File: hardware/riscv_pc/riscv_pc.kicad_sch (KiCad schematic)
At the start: 14 parts, among them J1 te_m.2_b, J2 te_m.2_b, J3 Conn_01x06, J4 HDMI_A, J5 AudioJack3, SW1 TS-1187A-C-D-B

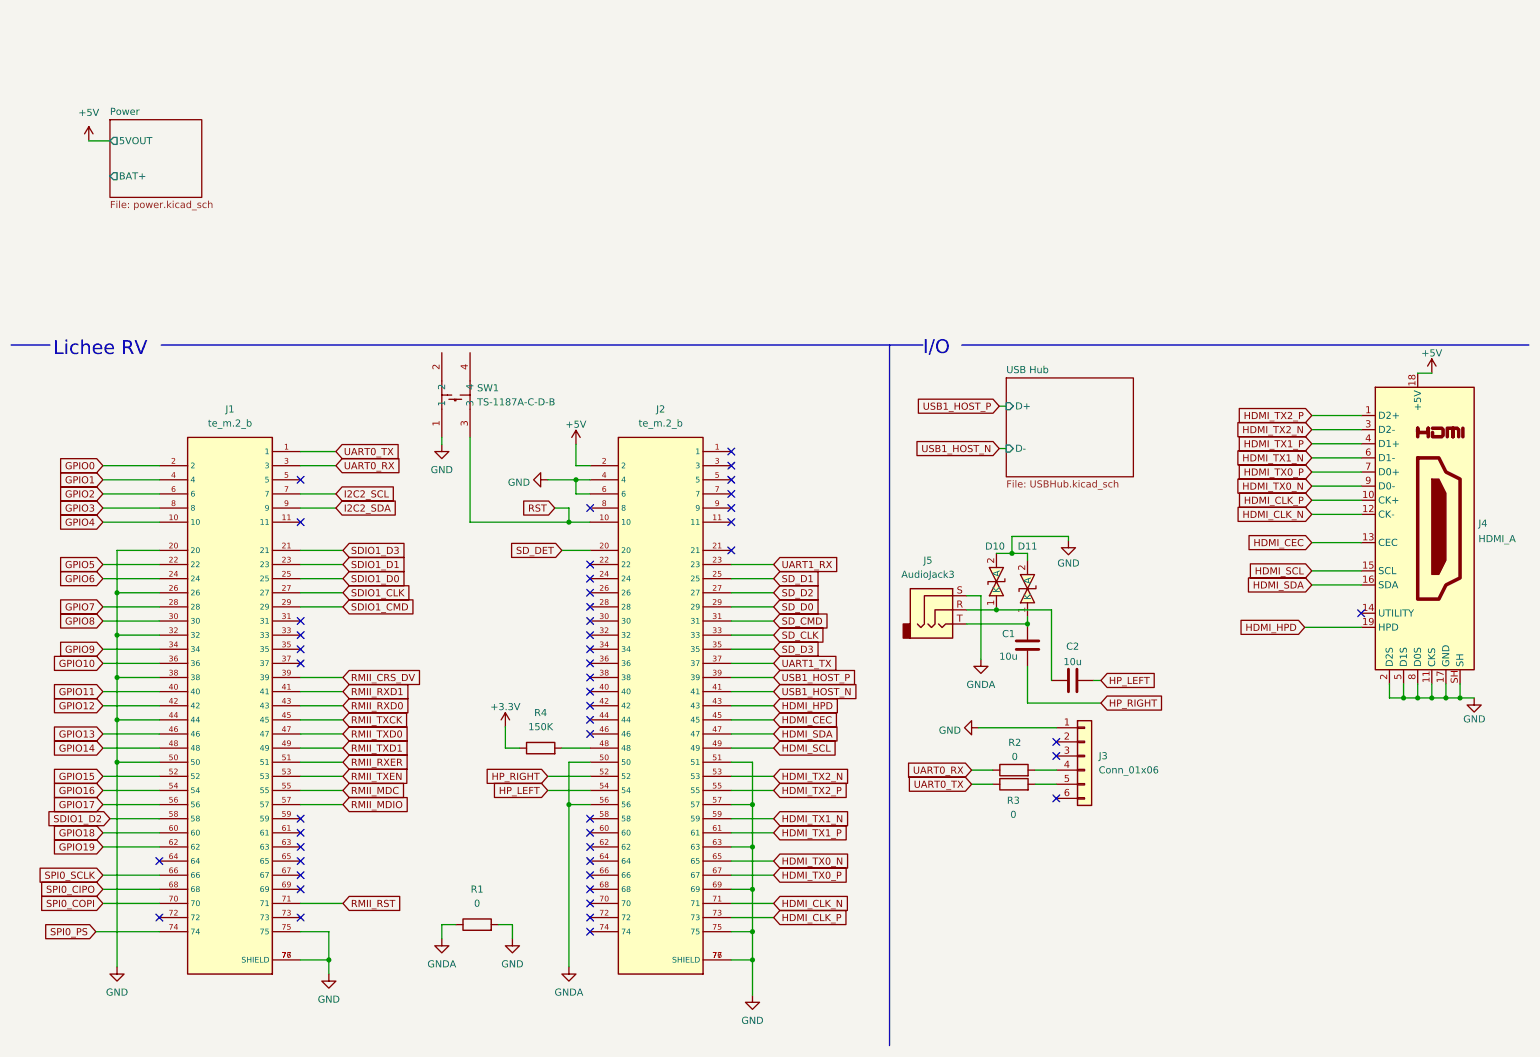
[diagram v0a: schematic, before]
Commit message: Add GPIO Header (2x15)
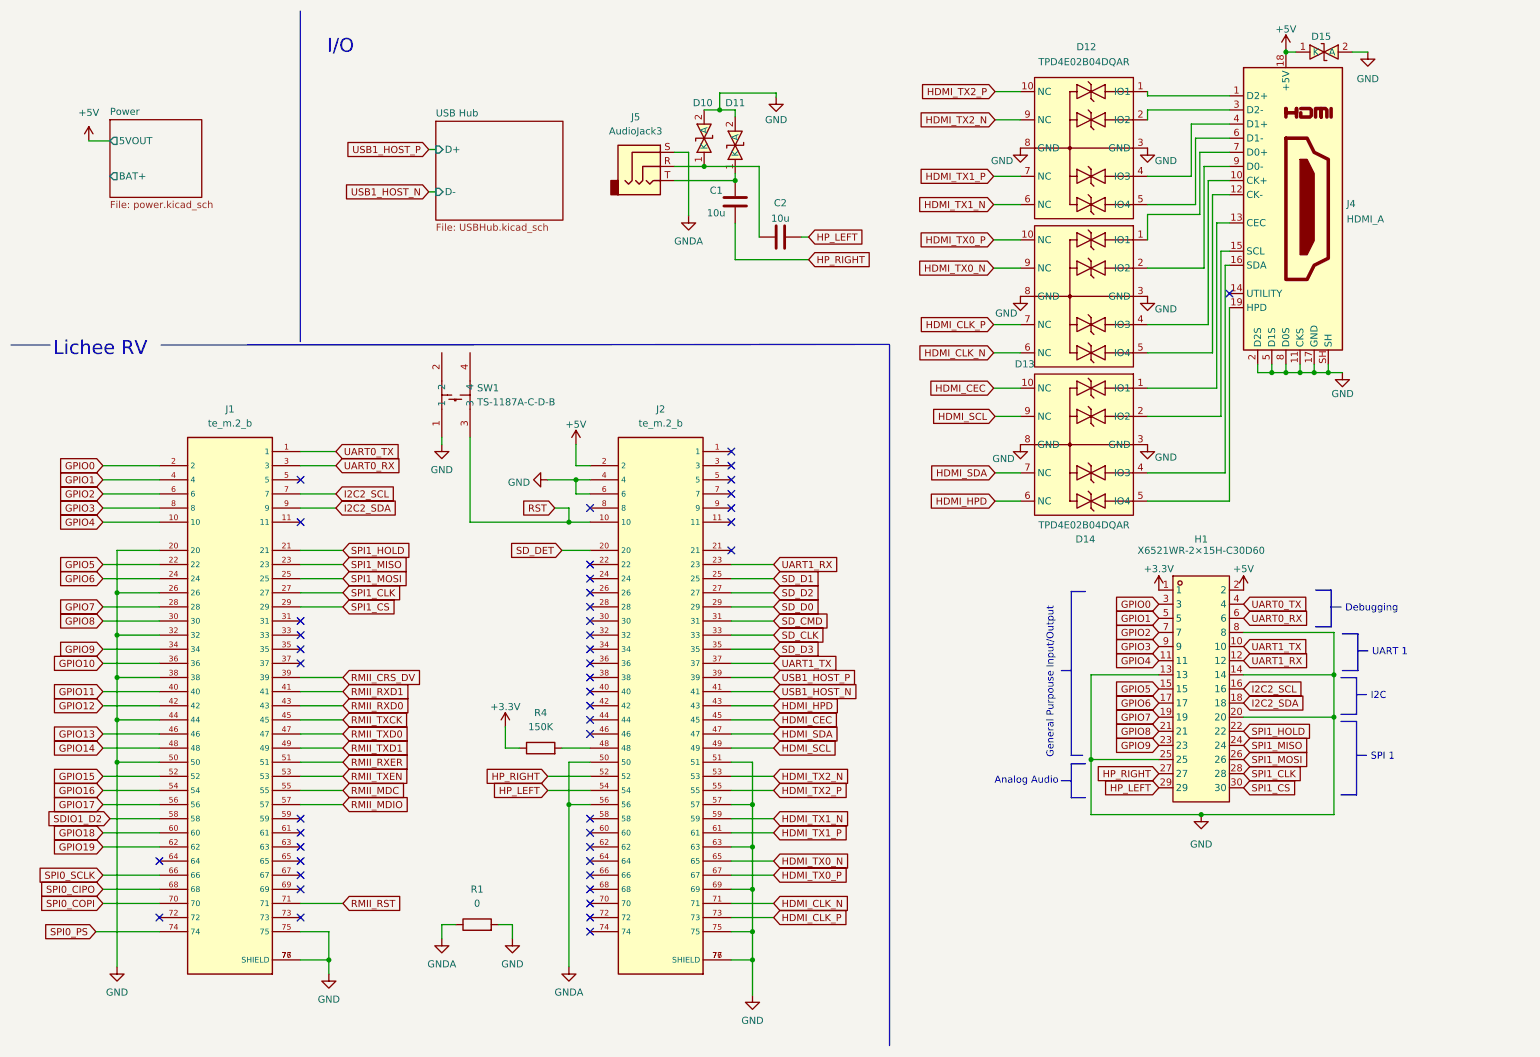
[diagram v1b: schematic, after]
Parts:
- removed J3: Conn_01x06, Connector_PinHeader_2.54mm:PinHeader_1x06_P2.54mm_Vertical, symbol Connector_Generic:Conn_01x06
- removed R2, R3: 0, Resistor_SMD:R_0603_1608Metric, symbol Device:R
- added D12, D13, D14: TPD4E02B04DQAR, easyeda2kicad:USON-10_L2.5-W1.0-P0.50-BL, symbol lcsc:TPD4E02B04DQAR
- added D15: GBLC08C-LF-T7, easyeda2kicad:SOD-323_L1.8-W1.3-LS2.5-BI, symbol lcsc:GBLC08C-LF-T7
- added H1: X6521WR-2×15H-C30D60, easyeda2kicad:HDR-TH_30P-P2.54-H-M-R2-C15-S2.54, symbol lcsc:X6521WR-2×15H-C30D60
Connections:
- net +5V: now also D15.1 (K), H1.2
- net GND: now also D12.3 (GND), D12.8 (GND), D13.3 (GND), D13.8 (GND), D14.3 (GND), D14.8 (GND), D15.2 (A), H1.13, H1.14, H1.20, H1.25, H1.8
- net GPIO0: now also H1.3
- net GPIO1: now also H1.5
- net GPIO2: now also H1.7
- net GPIO3: now also H1.9
- net GPIO4: now also H1.11
- net GPIO5: now also H1.15
- net GPIO6: now also H1.17
- net GPIO7: now also H1.19
- net GPIO8: now also H1.21
- net GPIO9: now also H1.23
- net HDMI_CEC: now also D14.10 (NC); no longer J4.13 (CEC)
- net HDMI_CLK_N: now also D13.6 (NC); no longer J4.12 (CK-)
- net HDMI_CLK_P: now also D13.7 (NC); no longer J4.10 (CK+)
- net HDMI_HPD: now also D14.6 (NC); no longer J4.19 (HPD)
- net HDMI_SCL: now also D14.9 (NC); no longer J4.15 (SCL)
- net HDMI_SDA: now also D14.7 (NC); no longer J4.16 (SDA)
- net HDMI_TX0_N: now also D13.9 (NC); no longer J4.9 (D0-)
- net HDMI_TX0_P: now also D13.10 (NC); no longer J4.7 (D0+)
- net HDMI_TX1_N: now also D12.6 (NC); no longer J4.6 (D1-)
- net HDMI_TX1_P: now also D12.7 (NC); no longer J4.4 (D1+)
- net HDMI_TX2_N: now also D12.9 (NC); no longer J4.3 (D2-)
- net HDMI_TX2_P: now also D12.10 (NC); no longer J4.1 (D2+)
- net HP_LEFT: now also H1.29
- net HP_RIGHT: now also H1.27
- net I2C2_SCL: now also H1.16
- net I2C2_SDA: now also H1.18
- net UART0_RX: now also H1.6
- net UART0_TX: now also H1.4
- net UART1_RX: now also H1.12
- net UART1_TX: now also H1.10
- net SDIO1_CLK renamed SPI1_CLK
- net SPI1_CLK: now also H1.28
- net SDIO1_CMD renamed SPI1_CS
- net SPI1_CS: now also H1.30
- net SDIO1_D0 renamed SPI1_MOSI
- net SPI1_MOSI: now also H1.26
- net SDIO1_D1 renamed SPI1_MISO
- net SPI1_MISO: now also H1.24
- net SDIO1_D3 renamed SPI1_HOLD
- net SPI1_HOLD: now also H1.22
- new net: D13.1 (IO1), J4.7 (D0+)
- new net: D13.2 (IO2), J4.9 (D0-)
- new net: D13.4 (IO3), J4.10 (CK+)
- new net: D13.5 (IO4), J4.12 (CK-)
- new net: D12.1 (IO1), J4.1 (D2+)
- new net: D14.1 (IO1), J4.13 (CEC)
- new net: D14.2 (IO2), J4.15 (SCL)
- new net: D14.4 (IO3), J4.16 (SDA)
- new net: D14.5 (IO4), J4.19 (HPD)
- new net: D12.2 (IO2), J4.3 (D2-)
- new net: D12.4 (IO3), J4.4 (D1+)
- new net: D12.5 (IO4), J4.6 (D1-)
- new net +3.3V: H1.1
- no-connect marks 49 -> 46
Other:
- note added: "Analog Audio"
- note added: "Debugging"
- note added: "General Purpouse Input/Output"
- note added: "I2C"
- note added: "SPI 1"
- note added: "UART 1"
- moved on the sheet: C1, C2, D10, D11, J4, J5
